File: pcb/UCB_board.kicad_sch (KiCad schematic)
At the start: 28 parts

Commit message: Cleaning
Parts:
- D1, D13, D14, D2, D4, D6: value ~ -> (none)

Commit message: Unify component values/footprints per checklist; add via-in-pad DRC rule; regenerate production outputs
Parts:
- D1, D13, D14, D2, D4, D6: value (none) -> FYLS-1206PGC; footprint LED_SMD:LED_0603_1608Metric_Pad1.05x0.95mm_HandSolder -> LED_SMD:LED_0603_1608Metric
- R23, R24, R25, R26: footprint Resistor_SMD:R_0402_1005Metric_Pad0.72x0.64mm_HandSolder -> Resistor_SMD:R_0402_1005Metric
- R86, R87: footprint Resistor_SMD:R_0603_1608Metric_Pad0.98x0.95mm_HandSolder -> Resistor_SMD:R_0603_1608Metric
- RN1: Manufacturer_Part_Number 4D03WGJ0103T5E -> 4D03WGJ0471T5E
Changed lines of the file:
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@@
 			)
 		)
-		(property "Value" ""
+		(property "Value" "FYLS-1206PGC"
 			(at 154.178 140.97 0)
 			(show_name no)
@@
 			)
 		)
-		(property "Footprint" "LED_SMD:LED_0603_1608Metric_Pad1.05x0.95mm_HandSolder"
+		(property "Footprint" "LED_SMD:LED_0603_1608Metric"
 			(at 151.13 137.16 0)
 			(hide yes)
@@
 			)
 		)
-		(property "Footprint" "Resistor_SMD:R_0402_1005Metric_Pad0.72x0.64mm_HandSolder"
+		(property "Footprint" "Resistor_SMD:R_0402_1005Metric"
 			(at 179.07 48.768 90)
 			(hide yes)
@@
 			)
 		)
-		(property "Value" ""
+		(property "Value" "FYLS-1206PGC"
 			(at 74.422 119.38 0)
 			(show_name no)
@@
 			)
 		)
-		(property "Footprint" "LED_SMD:LED_0603_1608Metric_Pad1.05x0.95mm_HandSolder"
+		(property "Footprint" "LED_SMD:LED_0603_1608Metric"
 			(at 77.47 123.19 0)
 			(hide yes)
@@
 			)
 		)
-		(property "Value" ""
+		(property "Value" "FYLS-1206PGC"
 			(at 64.262 119.38 0)
 			(show_name no)
@@
 			)
 		)
-		(property "Footprint" "LED_SMD:LED_0603_1608Metric_Pad1.05x0.95mm_HandSolder"
+		(property "Footprint" "LED_SMD:LED_0603_1608Metric"
 			(at 67.31 123.19 0)
 			(hide yes)
@@
 			)
 		)
-		(property "Footprint" "Resistor_SMD:R_0402_1005Metric_Pad0.72x0.64mm_HandSolder"
+		(property "Footprint" "Resistor_SMD:R_0402_1005Metric"
 			(at 179.07 43.688 90)
 			(hide yes)
@@
 			)
 		)
-		(property "Footprint" "Resistor_SMD:R_0603_1608Metric_Pad0.98x0.95mm_HandSolder"
+		(property "Footprint" "Resistor_SMD:R_0603_1608Metric"
 			(at 65.532 132.08 90)
 			(hide yes)
@@
 			)
 		)
-		(property "Footprint" "Resistor_SMD:R_0402_1005Metric_Pad0.72x0.64mm_HandSolder"
+		(property "Footprint" "Resistor_SMD:R_0402_1005Metric"
 			(at 179.07 51.308 90)
 			(hide yes)
@@
 			)
 		)
-		(property "Description" "4D03WGJ0103T5E"
+		(property "Description" "4D03WGJ0471T5E"
 			(at 153.67 149.86 0)
 			(hide yes)
@@
 			)
 		)
-		(property "Manufacturer_Part_Number" "4D03WGJ0103T5E"
+		(property "Manufacturer_Part_Number" "4D03WGJ0471T5E "
 			(at 153.67 149.86 90)
 			(hide yes)
@@
 			)
 		)
-		(property "Footprint" "Resistor_SMD:R_0603_1608Metric_Pad0.98x0.95mm_HandSolder"
+		(property "Footprint" "Resistor_SMD:R_0603_1608Metric"
 			(at 75.692 132.08 90)
 			(hide yes)
@@
 			)
 		)
-		(property "Value" ""
+		(property "Value" "FYLS-1206PGC"
 			(at 169.418 140.97 0)
 			(show_name no)
@@
 			)
 		)
-		(property "Footprint" "LED_SMD:LED_0603_1608Metric_Pad1.05x0.95mm_HandSolder"
+		(property "Footprint" "LED_SMD:LED_0603_1608Metric"
 			(at 166.37 137.16 0)
 			(hide yes)
@@
 			)
 		)
-		(property "Value" ""
+		(property "Value" "FYLS-1206PGC"
 			(at 146.558 140.97 0)
 			(show_name no)
@@
 			)
 		)
-		(property "Footprint" "LED_SMD:LED_0603_1608Metric_Pad1.05x0.95mm_HandSolder"
+		(property "Footprint" "LED_SMD:LED_0603_1608Metric"
 			(at 143.51 137.16 0)
 			(hide yes)
@@
 			)
 		)
-		(property "Value" ""
+		(property "Value" "FYLS-1206PGC"
 			(at 161.798 140.97 0)
 			(show_name no)
@@
 			)
 		)
-		(property "Footprint" "LED_SMD:LED_0603_1608Metric_Pad1.05x0.95mm_HandSolder"
+		(property "Footprint" "LED_SMD:LED_0603_1608Metric"
 			(at 158.75 137.16 0)
 			(hide yes)
@@
 			)
 		)
-		(property "Footprint" "Resistor_SMD:R_0402_1005Metric_Pad0.72x0.64mm_HandSolder"
+		(property "Footprint" "Resistor_SMD:R_0402_1005Metric"
 			(at 179.07 46.228 90)
 			(hide yes)

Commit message: Apply review checklist fixes, add fiducials, regenerate production outputs
- W5500 clock from MCU MCO1 by default (R80 fitted, R23 DNP)
- Firmware .ioc: I2C1_SCL moved to PB8 to match schematic
- 2 fiducials per side (hand assembly), zones refilled
- Restore DRC exclusions dropped from .kicad_pro on last save (59, unchanged set)
- README: status updated (ready for prototype order), renders and production links
- .gitignore: drop leftover RDE_board ibom.config.ini entry
- Regenerate BOM, PDFs, gerber zip, interactive BOM and 3D renders
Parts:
- added FID1, FID2, FID3, FID4: Fiducial, Fiducial:Fiducial_0.5mm_Mask1mm, symbol Mechanical:Fiducial
- R23, R24, R25, R26: now not fitted; now left out of the parts list

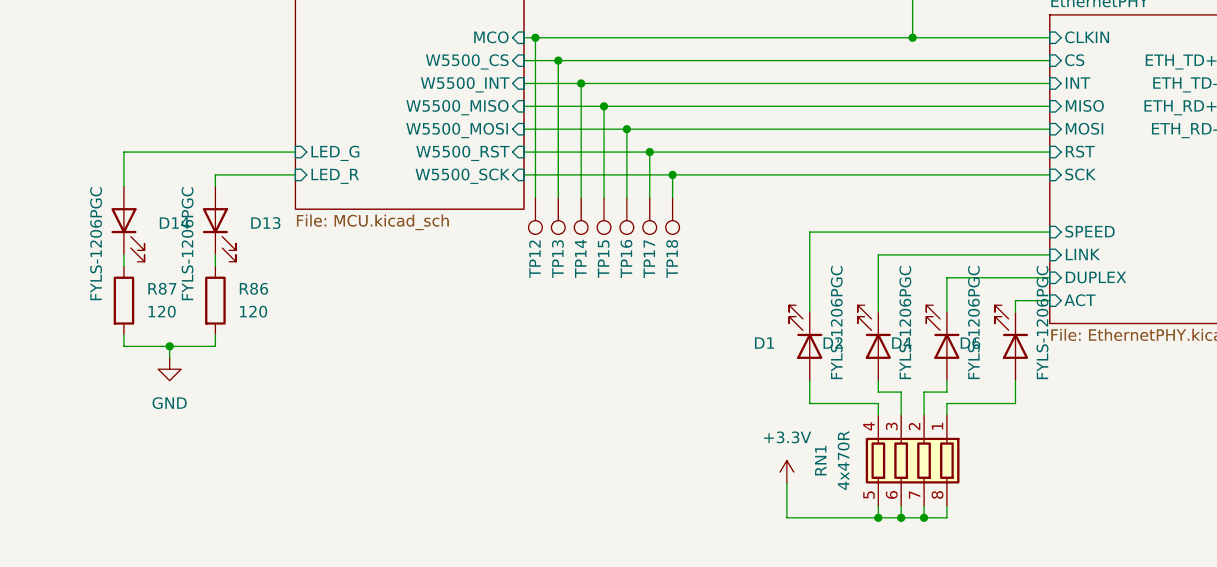
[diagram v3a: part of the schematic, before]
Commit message: Fix BOM data: 0603 LED part number (D1/D2/D4/D6/D13/D14), BOM field cleanup
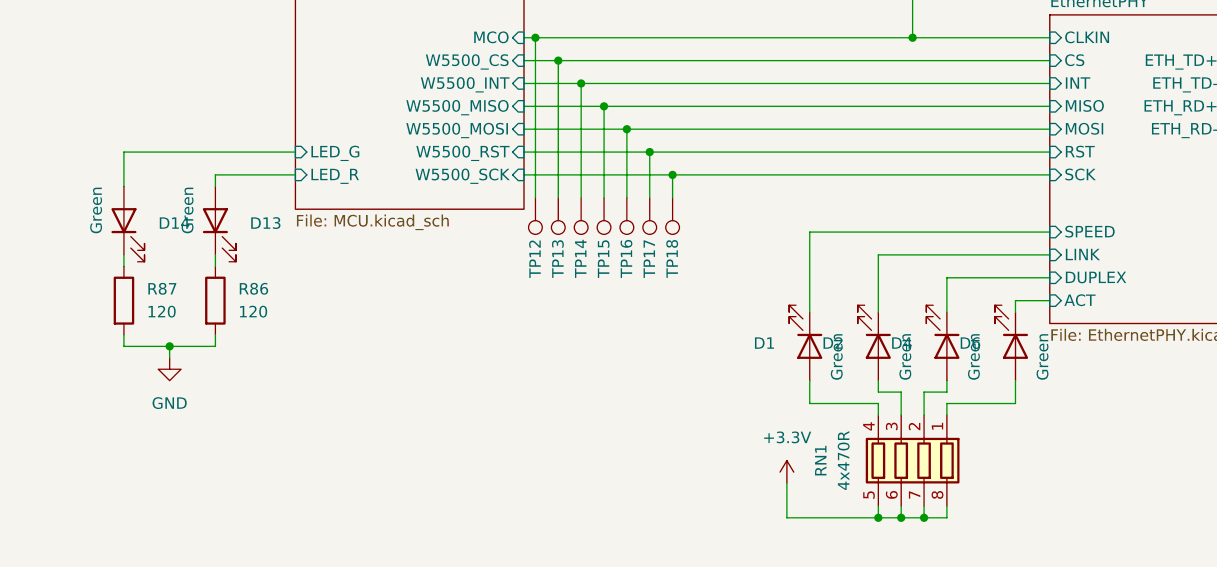
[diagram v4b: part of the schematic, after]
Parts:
- D1, D13, D14, D2, D4, D6: value FYLS-1206PGC -> Green; Manufacturer_Part_Number FYLS-1206PGC -> N0G69S04
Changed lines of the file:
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@@
 			)
 		)
-		(property "Value" "FYLS-1206PGC"
+		(property "Value" "Green"
 			(at 154.178 140.97 0)
 			(show_name no)
@@
 			)
 		)
-		(property "Manufacturer_Part_Number" "FYLS-1206PGC "
+		(property "Manufacturer_Part_Number" "N0G69S04"
 			(at 151.13 137.16 90)
 			(hide yes)
@@
 			)
 		)
-		(property "Value" "FYLS-1206PGC"
+		(property "Value" "Green"
 			(at 74.422 119.38 0)
 			(show_name no)
@@
 			)
 		)
-		(property "Manufacturer_Part_Number" "FYLS-1206PGC "
+		(property "Manufacturer_Part_Number" "N0G69S04"
 			(at 77.47 123.19 90)
 			(hide yes)
@@
 			)
 		)
-		(property "Value" "FYLS-1206PGC"
+		(property "Value" "Green"
 			(at 64.262 119.38 0)
 			(show_name no)
@@
 			)
 		)
-		(property "Manufacturer_Part_Number" "FYLS-1206PGC "
+		(property "Manufacturer_Part_Number" "N0G69S04"
 			(at 67.31 123.19 90)
 			(hide yes)
@@
 			)
 		)
-		(property "Description" "4D03WGJ0471T5E"
+		(property "Description" "Resistor array"
 			(at 153.67 149.86 0)
 			(hide yes)
@@
 			)
 		)
-		(property "Value" "FYLS-1206PGC"
+		(property "Value" "Green"
 			(at 169.418 140.97 0)
 			(show_name no)
@@
 			)
 		)
-		(property "Manufacturer_Part_Number" "FYLS-1206PGC "
+		(property "Manufacturer_Part_Number" "N0G69S04"
 			(at 166.37 137.16 90)
 			(hide yes)
@@
 			)
 		)
-		(property "Value" "FYLS-1206PGC"
+		(property "Value" "Green"
 			(at 146.558 140.97 0)
 			(show_name no)
@@
 			)
 		)
-		(property "Manufacturer_Part_Number" "FYLS-1206PGC "
+		(property "Manufacturer_Part_Number" "N0G69S04"
 			(at 143.51 137.16 90)
 			(hide yes)
@@
 			)
 		)
-		(property "Value" "FYLS-1206PGC"
+		(property "Value" "Green"
 			(at 161.798 140.97 0)
 			(show_name no)
@@
 			)
 		)
-		(property "Manufacturer_Part_Number" "FYLS-1206PGC "
+		(property "Manufacturer_Part_Number" "N0G69S04"
 			(at 158.75 137.16 90)
 			(hide yes)
